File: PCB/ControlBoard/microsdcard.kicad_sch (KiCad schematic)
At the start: 5 parts, among them J4 microSD, Q2 Q_PMOS_GSD

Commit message: First pass of PCB rework.
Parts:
- C11: footprint Capacitor_SMD:C_0805_2012Metric -> Capacitor_SMD:C_0603_1608Metric
- J4: footprint (none) -> KTANE:GCT_MEM2075-00-140-01-A; symbol Connector:Micro_SD_Card_Det2 -> Connector:Micro_SD_Card_Det1
- Q2: footprint (none) -> Package_TO_SOT_SMD:SOT-23
- R3, R7: footprint Resistor_SMD:R_0805_2012Metric -> Resistor_SMD:R_0603_1608Metric
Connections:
- net GND: now also J4.10 (SHIELD); no longer J4.11 (SHIELD), J4.9 (DET_B)
- net SD-DET: now also J4.9 (DET); no longer J4.10 (DET_A)

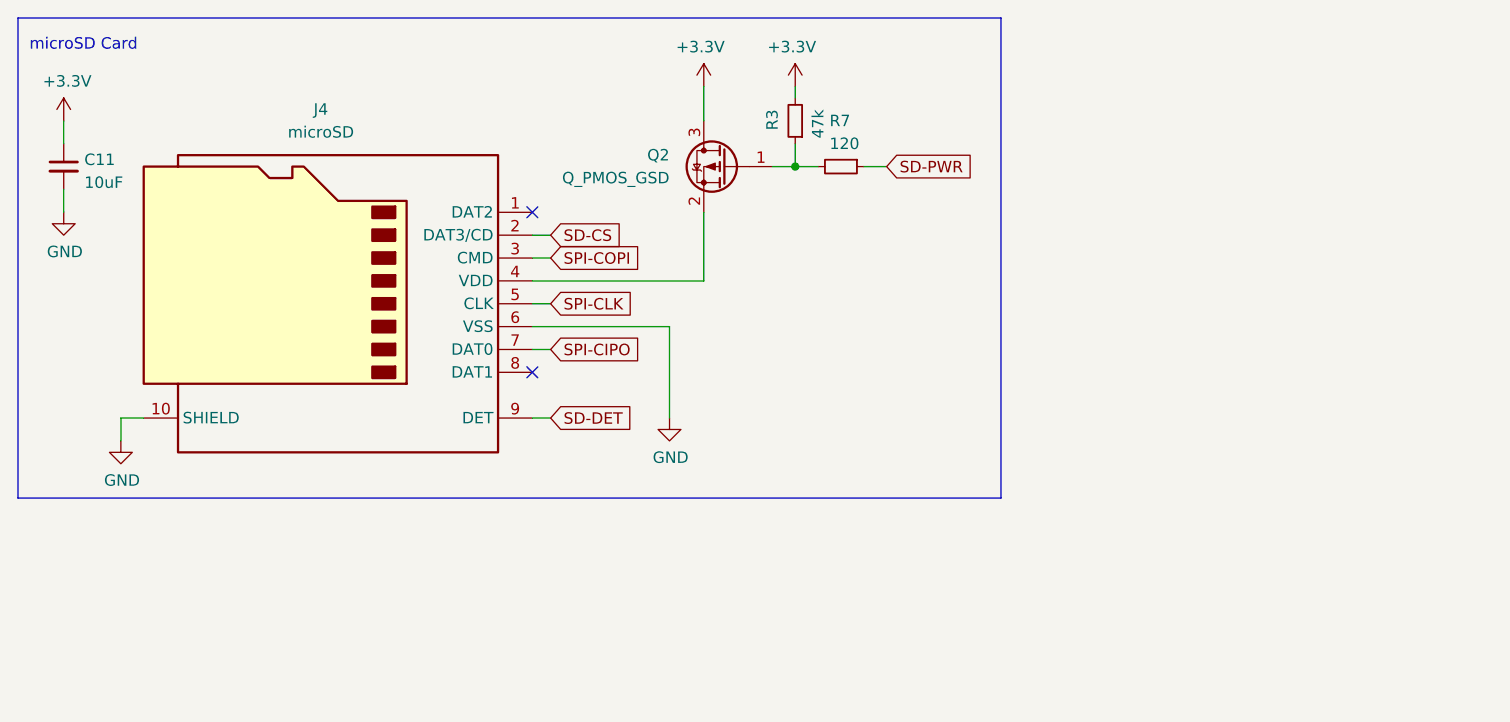
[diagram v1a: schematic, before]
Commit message: ControlBoard B02, with buck regulator fix.
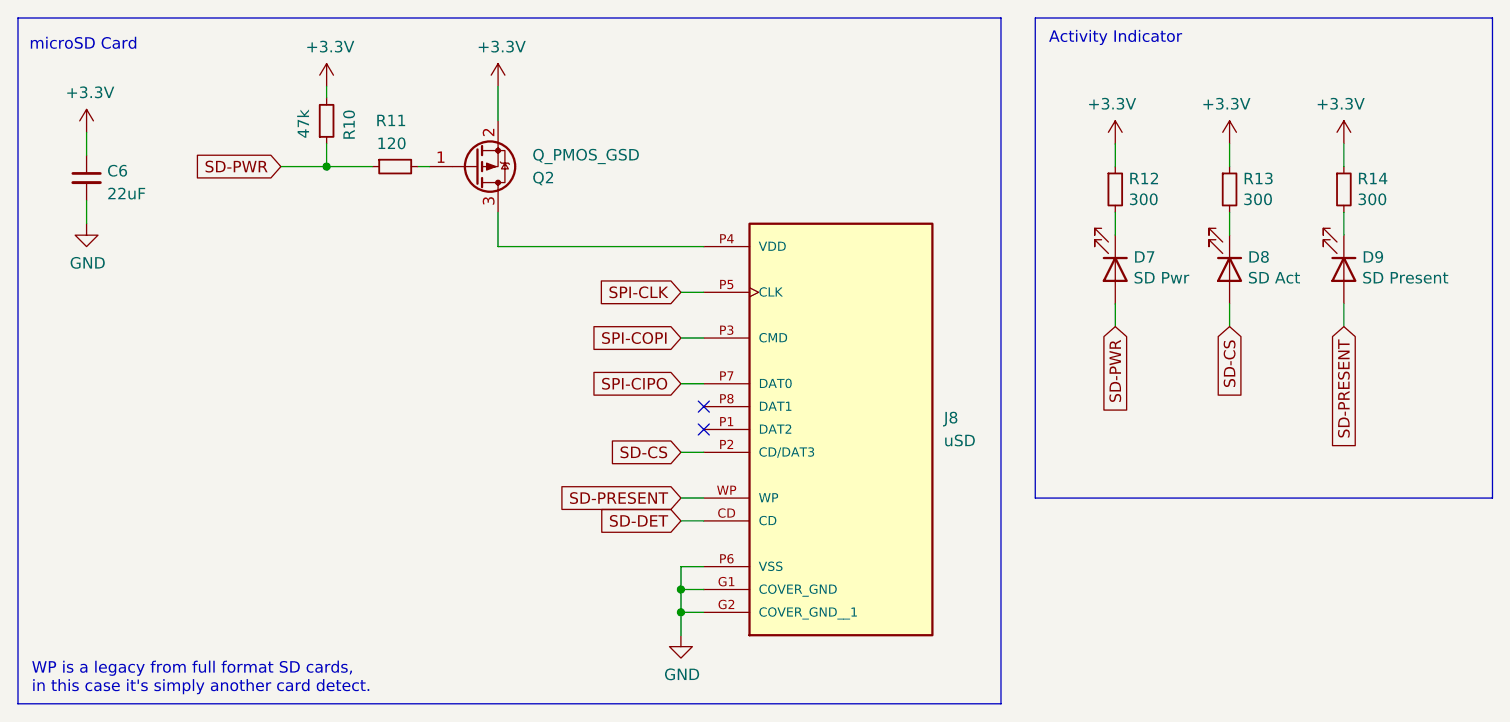
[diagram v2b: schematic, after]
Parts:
- removed C11: 10uF, Capacitor_SMD:C_0603_1608Metric, symbol Device:C_Small
- removed J4: microSD, KTANE:GCT_MEM2075-00-140-01-A, symbol Connector:Micro_SD_Card_Det1
- added C6: 22uF, Capacitor_SMD:C_0603_1608Metric, symbol Device:C_Small
- added D7: SD Pwr, LED_SMD:LED_0603_1608Metric, symbol Device:LED
- added D8: SD Act, LED_SMD:LED_0603_1608Metric, symbol Device:LED
- added D9: SD Present, LED_SMD:LED_0603_1608Metric, symbol Device:LED
- added J8: uSD, KTANE:CUI_MSD-11-A, symbol KTANE:MSD-11-A
- added R12, R13, R14: 300, Resistor_SMD:R_0603_1608Metric, symbol Device:R_Small
- renumbered R3 to R10, R7 to R11
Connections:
- net +3.3V: now also Q2.2 (S), C6.1, R12.1, R13.1, R14.1; no longer Q2.3 (D)
- net GND: now also C6.2, J8.G1 (COVER_GND), J8.G2 (COVER_GND__1), J8.P6 (VSS)
- net SD-CS: now also D8.2 (A), J8.P2 (CD/DAT3)
- net SD-DET: now also J8.CD
- net SD-PWR: now also R10.1, D7.2 (A)
- net SPI-CIPO: now also J8.P7 (DAT0)
- net SPI-CLK: now also J8.P5 (CLK)
- net SPI-COPI: now also J8.P3 (CMD)
- net at Q2.1 (G), R11.2: no longer R10.1
- new net: D9.1 (K), R14.2
- new net: J8.P4 (VDD), Q2.3 (D)
- new net: D8.1 (K), R13.2
- new net: D7.1 (K), R12.2
- new net SD-PRESENT: D9.2 (A), J8.WP
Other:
- note added: "Activity Indicator"
- note added: "WP is a legacy from full format SD cards, in this case it's simply another card detect."
- moved on the sheet: Q2, R10, R11
